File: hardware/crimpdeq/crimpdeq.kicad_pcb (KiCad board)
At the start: 2 copper layers, 52 parts, among them J2 USB4105-GF-A, Q1 S8550, Q2 DMG3415U, SW1 SW_Push, SW2 SW_Push, U1 ESP32-C3-MINI-1, U2 MCP73831T-2ACI/OT, U3 HX711, U4 Rust_Board, U6 SY8088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

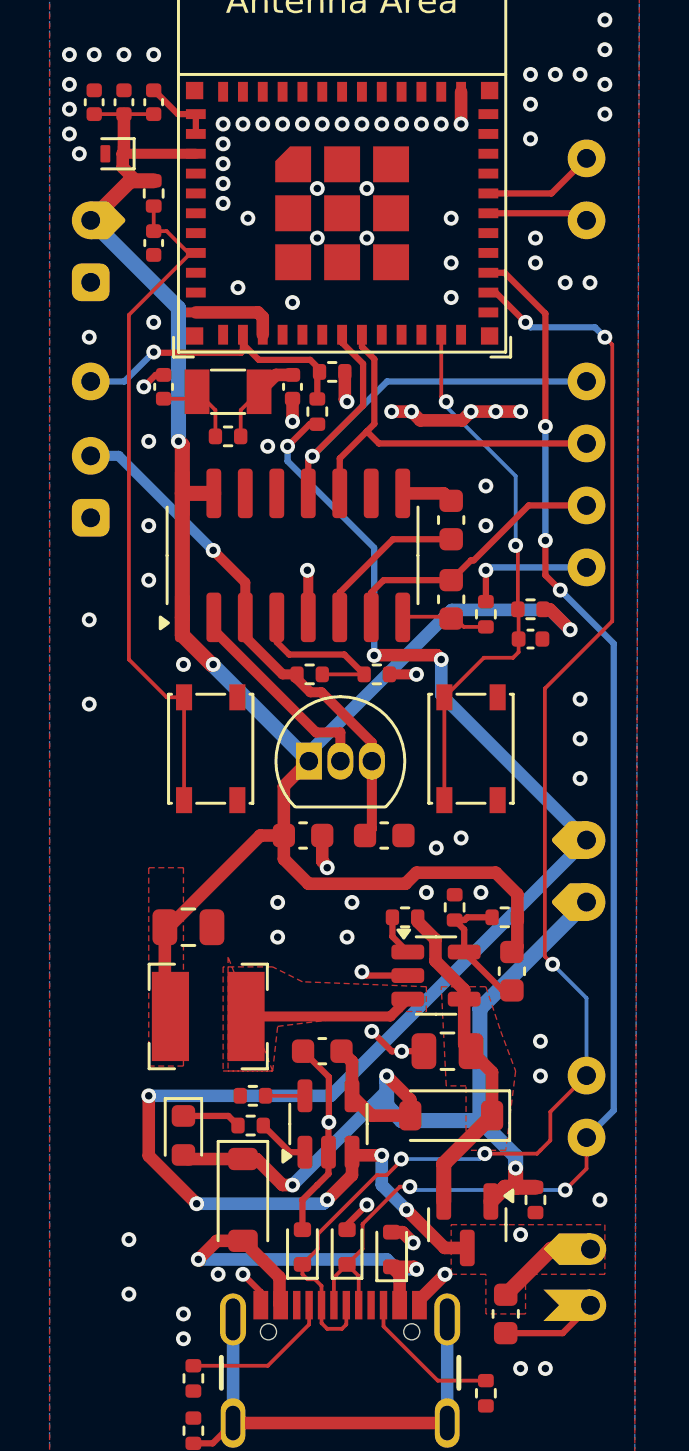
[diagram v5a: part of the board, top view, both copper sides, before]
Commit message: pcb: More DRC fixes
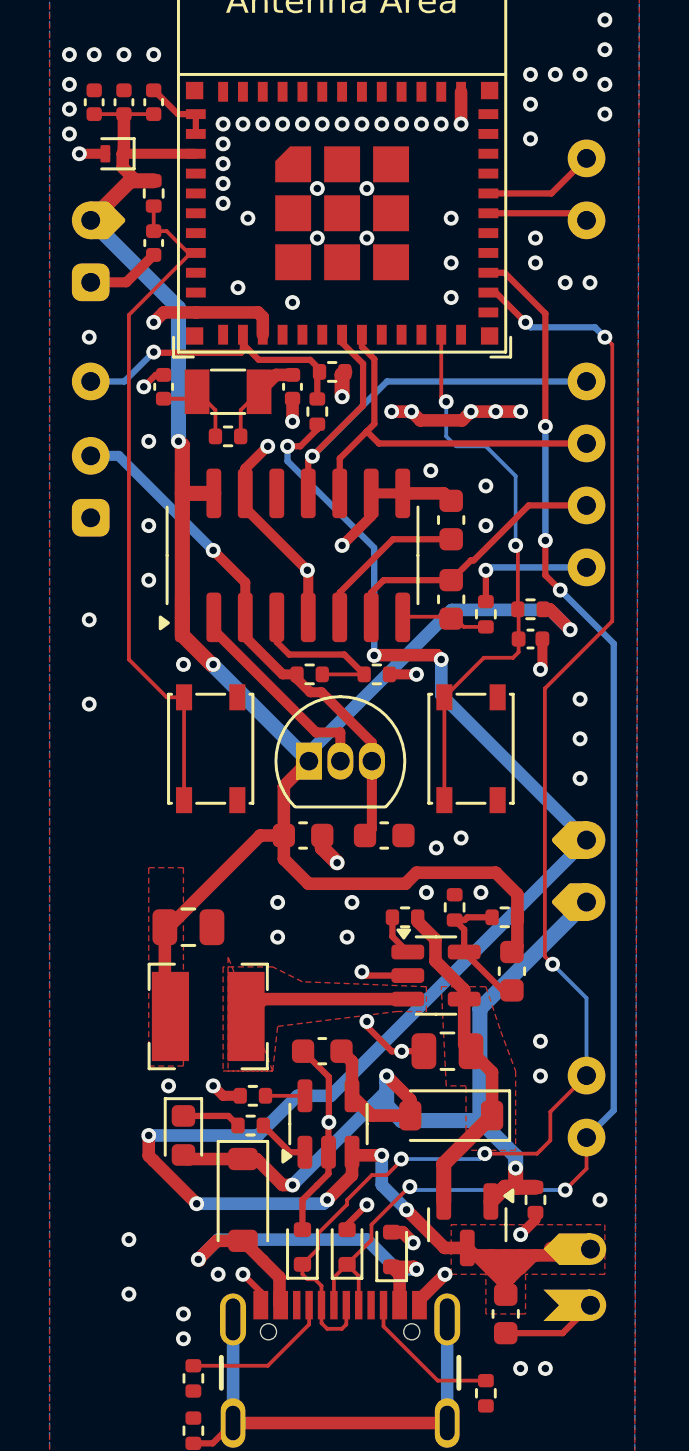
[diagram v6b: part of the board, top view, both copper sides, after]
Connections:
- U1 pad 49: (no net) -> GND
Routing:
- net GND: track 45.7 -> 65.8 mm, vias 100 -> 105
- net +BATT: track 69.8 -> 80.8 mm
- net IO9_BOOT: track 22.0 -> 22.7 mm
- net Net-(D8-A): track 17.1 -> 17.8 mm
